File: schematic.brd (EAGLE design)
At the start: 160 x 100 mm, 26 parts, among them IC1 AD8015

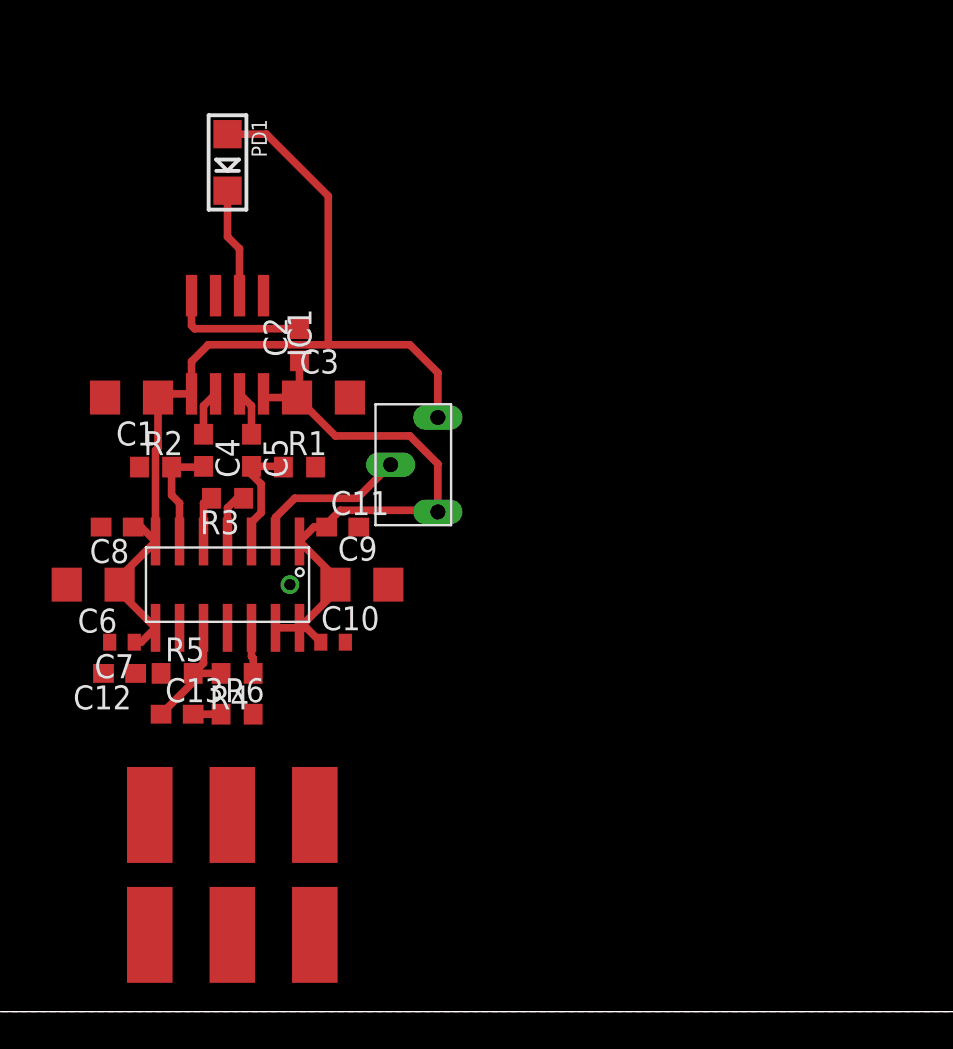
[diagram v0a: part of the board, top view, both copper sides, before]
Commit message: Fixed DRC Error and second circuit
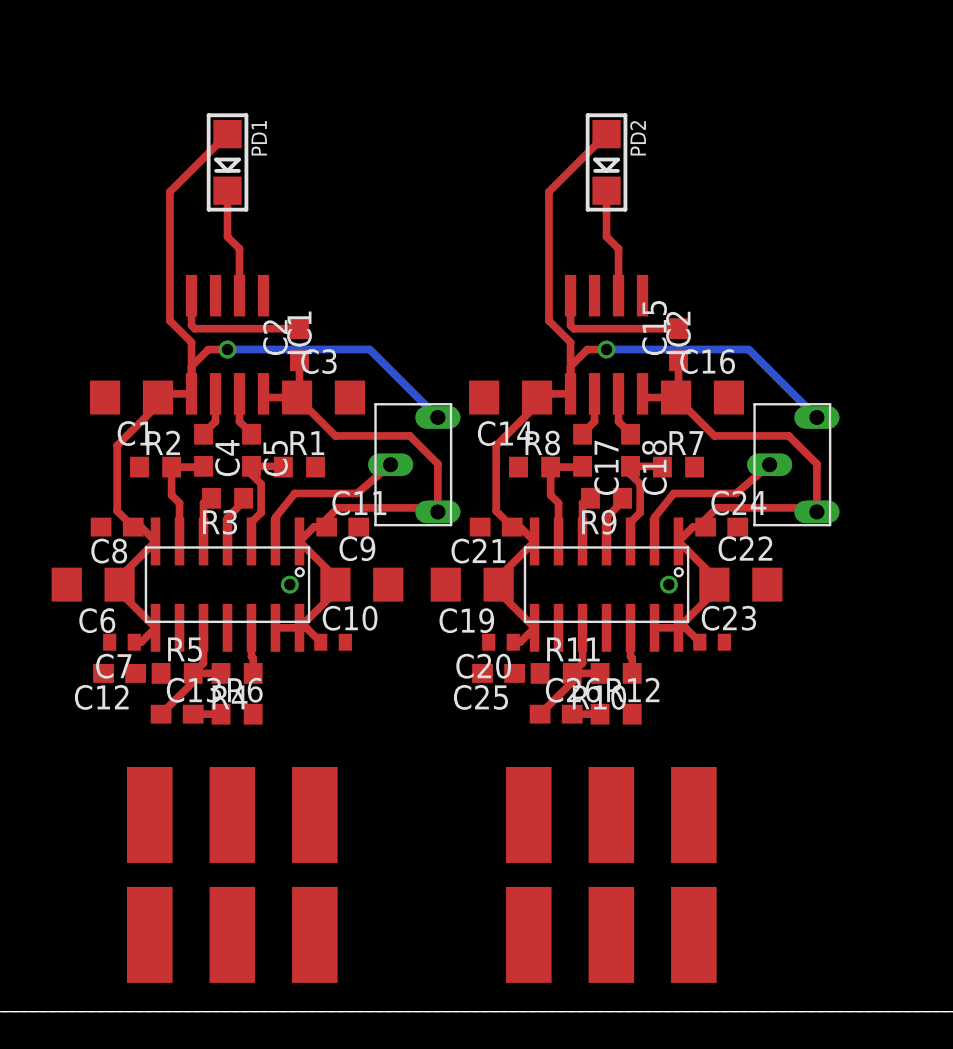
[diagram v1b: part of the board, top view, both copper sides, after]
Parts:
- added C14, C16, C19, C22: 6.8uF, rcl:C1206
- added C15, C17, C18: .1uF, rcl:C0603
- added C20, C23: 0.1uF, rcl:C0402
- added C21, C24, C26: 0.1uF, rcl:C0603
- added C25: 39pF, rcl:C0603
- added IC2: AD8015, analog-devices:SO8
- added PD2: (no value), microbuilder:CHIPLED_1206
- added R10: 1k, rcl:R0603
- added R11, R12, R9: 100, rcl:R0603
- added R7, R8: 50, rcl:R0603
- added U$6: LMH6503, 12-ChannelEMG:SOIC14
- added U$7: PV37W, 12-ChannelEMG:PV37W
- added U$8, U$9: BNCCONN, 12-ChannelEMG:BNCPADS
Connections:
- new net N$15: C15.2, IC2.4
- new net N$16: IC2.2, PD2.C
- new net N$17: C18.1, IC2.7
- new net N$18: C17.1, IC2.6
- new net N$19: C17.2, R8.2, U$6.6
- new net N$20: C18.2, R7.1, U$6.3
- new net N$21: R9.1, U$6.4
- new net N$22: R9.2, U$6.5
- new net N$23: R10.1, U$6.12
- new net N$24: C26.1, R10.2, R11.2, U$6.10
- new net N$25: C25.1, R11.1
- new net N$26: C26.2, R12.1
- new net N$27: U$6.2, U$7.2, U$8.2
- new net N$28: R12.2, U$9.2
- net +5V: now also C15.1, C16.1, C22.1, C23.1, C24.1, IC2.8, U$6.1, U$6.13, U$6.14, U$7.1
- net -5V: now also C14.1, C19.1, C20.1, C21.1, IC2.5, PD2.A, U$6.7, U$6.8, U$7.3
- net GND: now also C14.2, C16.2, C19.2, C20.2, C21.2, C22.2, C23.2, C24.2, C25.2, R7.2, R8.1, U$6.11, U$6.9, U$8.1, U$8.3, U$9.1, U$9.3
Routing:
- net -5V: track 51.4 -> 102.0 mm, vias 0 -> 2
- net +5V: track 32.3 -> 65.4 mm
- net N$27: track 0.00 -> 8.54 mm
- net N$15: track 0.00 -> 7.37 mm
- net N$24: track 0.00 -> 6.98 mm
- net N$20: track 0.00 -> 6.10 mm
- net N$16: track 0.00 -> 5.82 mm
- net N$19: track 0.00 -> 5.82 mm
- net N$21: track 0.00 -> 3.15 mm
- net N$22: track 0.00 -> 2.56 mm
- net N$23: track 0.00 -> 2.45 mm
- net N$18: track 0.00 -> 2.40 mm
- net N$17: track 0.00 -> 2.40 mm
- net N$26: track 0.00 -> 1.47 mm

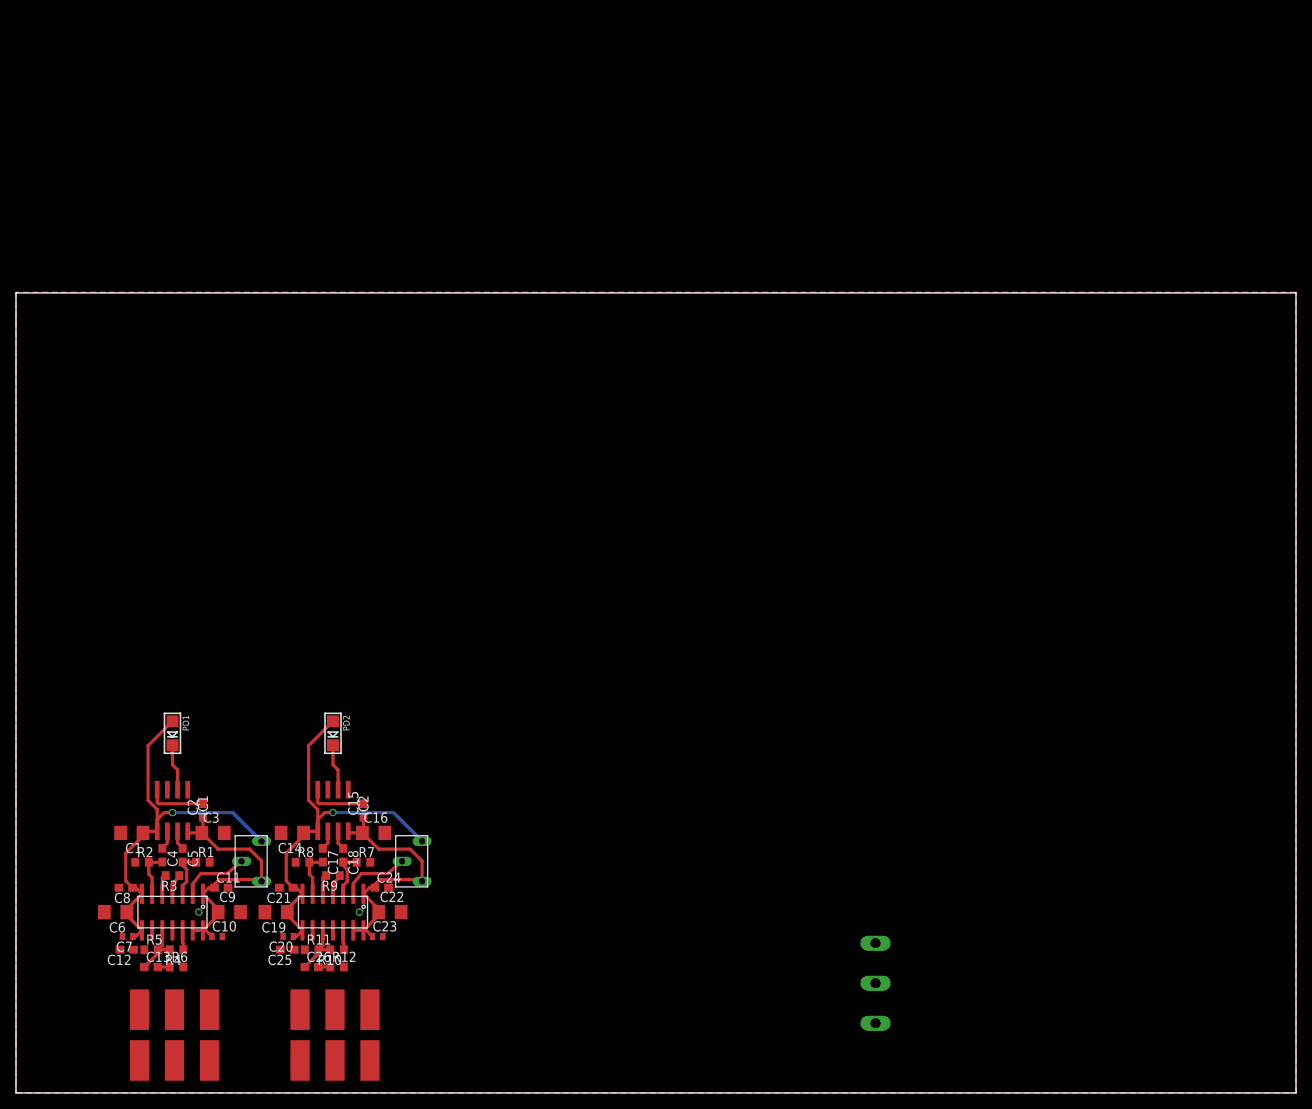
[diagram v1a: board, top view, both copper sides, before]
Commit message: Added rest of copies and wired everything together.
Need to add silkscreen and fix photo diodes
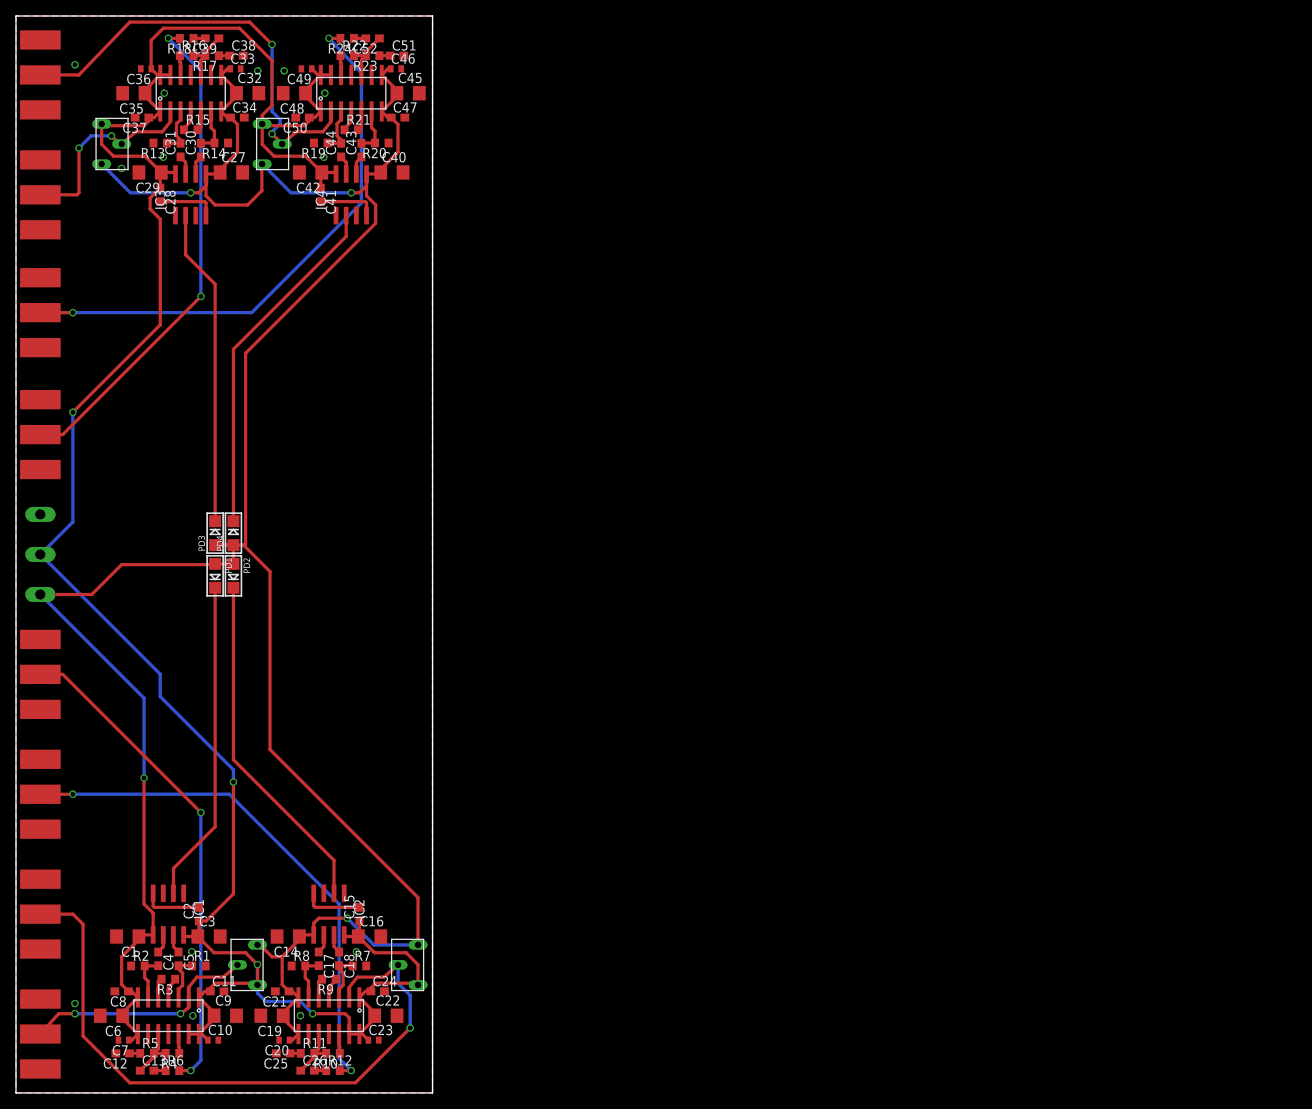
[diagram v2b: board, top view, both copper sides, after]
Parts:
- added C27, C29, C32, C35, C40, C42, C45, C48: 6.8uF, rcl:C1206
- added C28, C30, C31, C41, C43, C44: .1uF, rcl:C0603
- added C33, C36, C46, C49: 0.1uF, rcl:C0402
- added C34, C37, C39, C47, C50, C52: 0.1uF, rcl:C0603
- added C38, C51: 39pF, rcl:C0603
- added IC3, IC4: AD8015, analog-devices:SO8
- added PD3, PD4: (no value), microbuilder:CHIPLED_1206
- added R13, R14, R19, R20: 50, rcl:R0603
- added R15, R17, R18, R21, R23, R24: 100, rcl:R0603
- added R16, R22: 1k, rcl:R0603
- added U$10, U$14: LMH6503, 12-ChannelEMG:SOIC14
- added U$11, U$15: PV37W, 12-ChannelEMG:PV37W
- added U$12, U$13, U$16, U$17: BNCCONN, 12-ChannelEMG:BNCPADS
- moved U$3 117.3 mm to (3.05, 67.3)
- moved U$5 51.1 mm to (3.05, 52.3), turned to 90 degrees
- moved U$9 49.6 mm to (3.05, 37.3), turned to 90 degrees
- moved U$8 38.7 mm to (3.05, 22.4), turned to 90 degrees
- moved PD2 23.3 mm to (27.2, 64.6)
- moved PD1 20.4 mm to (24.9, 64.6)
- moved U$4 17.0 mm to (3.05, 7.37), turned to 90 degrees
- moved C19 13.0 mm to (32.0, 9.65)
- moved C22 13.0 mm to (46.2, 9.65)
- moved C6 13.0 mm to (11.9, 9.65)
- moved C9 13.0 mm to (26.2, 9.65)
- moved U$1 13.0 mm to (19.1, 9.65)
- moved U$6 13.0 mm to (39.1, 9.65)
- moved C1 13.0 mm to (14.0, 19.6)
- moved C10 13.0 mm to (24.6, 6.60)
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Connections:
- new net N$29: C28.2, IC3.4
- new net N$30: IC3.2, PD3.C
- new net N$31: C31.1, IC3.7
- new net N$32: C30.1, IC3.6
- new net N$33: C30.2, R14.2, U$10.6
- new net N$34: C31.2, R13.1, U$10.3
- new net N$35: R15.1, U$10.4
- new net N$36: R15.2, U$10.5
- new net N$37: R16.1, U$10.12
- new net N$38: C39.1, R16.2, R17.2, U$10.10
- new net N$39: C38.1, R17.1
- new net N$40: C39.2, R18.1
- new net N$41: U$10.2, U$11.2, U$12.2
- new net N$42: R18.2, U$13.2
- new net N$43: C41.2, IC4.4
- new net N$44: IC4.2, PD4.C
- new net N$45: C44.1, IC4.7
- new net N$46: C43.1, IC4.6
- new net N$47: C43.2, R20.2, U$14.6
- new net N$48: C44.2, R19.1, U$14.3
- new net N$49: R21.1, U$14.4
- new net N$50: R21.2, U$14.5
- new net N$51: R22.1, U$14.12
- new net N$52: C52.1, R22.2, R23.2, U$14.10
- new net N$53: C51.1, R23.1
- new net N$54: C52.2, R24.1
- new net N$55: U$14.2, U$15.2, U$16.2
- new net N$56: R24.2, U$17.2
- net +5V: now also C28.1, C29.1, C35.1, C36.1, C37.1, C41.1, C42.1, C48.1, C49.1, C50.1, IC3.8, IC4.8, U$10.1, U$10.13, U$10.14, U$11.1, U$14.1, U$14.13, U$14.14, U$15.1
- net -5V: now also C27.1, C32.1, C33.1, C34.1, C40.1, C45.1, C46.1, C47.1, IC3.5, IC4.5, PD3.A, PD4.A, U$10.7, U$10.8, U$11.3, U$14.7, U$14.8, U$15.3
- net GND: now also C27.2, C29.2, C32.2, C33.2, C34.2, C35.2, C36.2, C37.2, C38.2, C40.2, C42.2, C45.2, C46.2, C47.2, C48.2, C49.2, C50.2, C51.2, R13.2, R14.1, R19.2, R20.1, U$10.11, U$10.9, U$12.1, U$12.3, U$13.1, U$13.3, U$14.11, U$14.9, U$16.1, U$16.3, U$17.1, U$17.3
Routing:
- net -5V: track 102.0 -> 338.6 mm, vias 2 -> 4
- net +5V: track 65.4 -> 289.7 mm, vias 0 -> 4
- net N$27: track 8.54 -> 83.0 mm, vias 0 -> 1
- net N$56: track 0.00 -> 69.4 mm, vias 0 -> 2
- net N$28: track 0.00 -> 65.9 mm, vias 0 -> 2
- net N$42: track 0.00 -> 62.6 mm, vias 0 -> 2
- net N$14: track 0.00 -> 61.4 mm, vias 0 -> 2
- net N$55: track 0.00 -> 55.3 mm, vias 0 -> 2
- net N$44: track 0.00 -> 44.0 mm
- net N$30: track 0.00 -> 39.7 mm
- net N$16: track 5.82 -> 43.4 mm
- net N$1: track 5.82 -> 40.4 mm
- net N$41: track 0.00 -> 25.4 mm, vias 0 -> 2
- net N$13: track 8.54 -> 29.7 mm, vias 0 -> 2
- net N$29: track 0.00 -> 7.37 mm
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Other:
- board size 160 x 100 mm -> 52.1 x 134.6 mm

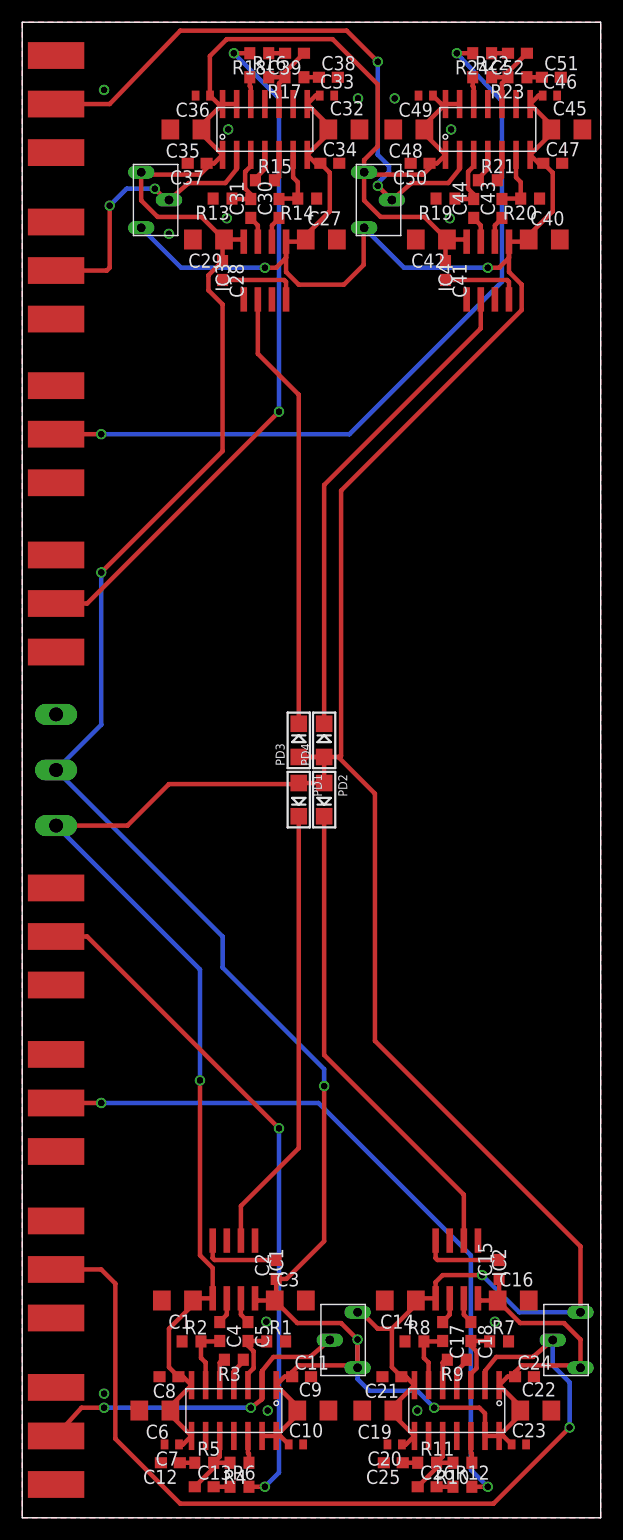
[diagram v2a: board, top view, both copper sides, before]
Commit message: Reorganized board to reduce parasitic factors.
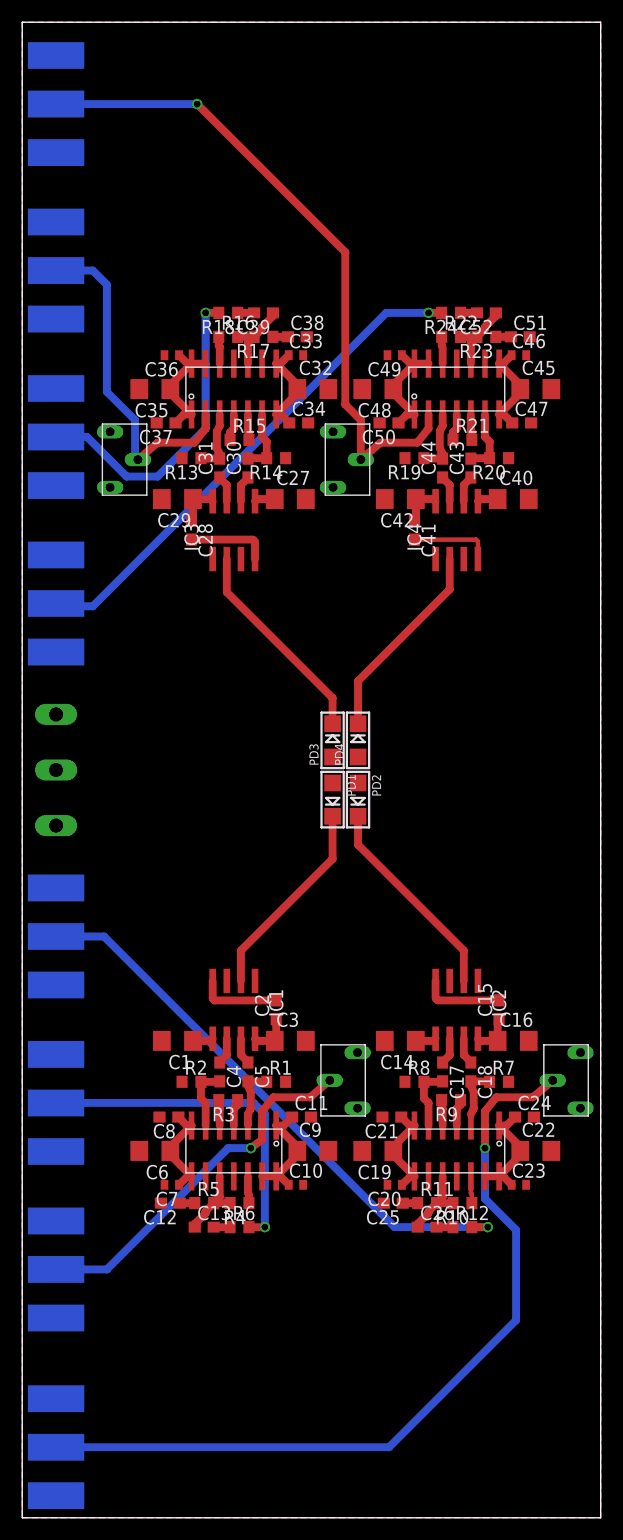
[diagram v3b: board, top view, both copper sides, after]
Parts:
- moved C32 23.5 mm to (26.2, 101.6)
- moved C35 23.5 mm to (11.9, 101.6)
- moved C45 23.5 mm to (46.2, 101.6)
- moved C48 23.5 mm to (32.0, 101.6)
- moved R13 23.5 mm to (15.2, 95.4)
- moved R14 23.5 mm to (22.9, 95.4)
- moved R19 23.5 mm to (35.3, 95.4)
- moved R20 23.5 mm to (42.9, 95.4)
- moved U$10 23.5 mm to (19.1, 101.6)
- moved U$14 23.5 mm to (39.1, 101.6)
- moved C27 23.5 mm to (24.1, 91.7)
- moved C28 23.5 mm to (15.2, 88.9)
- moved C29 23.5 mm to (14.0, 91.7)
- moved C30 23.5 mm to (20.3, 94.5)
- moved C31 23.5 mm to (17.8, 94.5)
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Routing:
- net -5V: track 338.6 -> 43.8 mm, vias 4 -> 0
- net +5V: track 289.7 -> 57.9 mm, vias 4 -> 0
- net N$42: track 62.6 -> 28.3 mm, vias 2 -> 1
- net N$14: track 61.4 -> 32.5 mm, vias 2 -> 1
- net N$44: track 44.0 -> 18.2 mm
- net N$16: track 43.4 -> 18.8 mm
- net N$56: track 69.4 -> 45.8 mm, vias 2 -> 1
- net N$1: track 40.4 -> 18.2 mm
- net N$30: track 39.7 -> 18.8 mm
- net N$28: track 65.9 -> 51.1 mm, vias 2 -> 1
- net N$27: track 83.0 -> 73.4 mm
- net N$41: track 25.4 -> 30.5 mm, vias 2 -> 0
- net N$55: track 55.3 -> 59.3 mm, vias 2 -> 1
- net N$13: track 29.7 -> 33.1 mm, vias 2 -> 1
